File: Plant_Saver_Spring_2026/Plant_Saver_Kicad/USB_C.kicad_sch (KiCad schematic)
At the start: 3 parts, among them J3 54-00284

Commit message: Footprint correction
Changed the DHT20 from a header pin to the recommended SIP. Also had to reannotate in order to assign footprints.
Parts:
- removed J3: 54-00284, 54-00284:TENSILITY_54-00284, symbol USB-C Female Port:54-00284
- removed R32, R33: 5.1K, Resistor_THT:R_Axial_DIN0207_L6.3mm_D2.5mm_P10.16mm_Horizontal, symbol Device:R_US

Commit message: Fixed USB-C and Linear Regulator Sheetfiles
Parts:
- added J3: 54-00284, 54-00284:TENSILITY_54-00284, symbol USB-C Female Port:54-00284
- added R32, R33: 5.1K, Resistor_THT:R_Axial_DIN0207_L6.3mm_D2.5mm_P10.16mm_Horizontal, symbol Device:R_US
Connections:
- new net: J3.A5 (CC1), R32.1
- new net: J3.B5 (CC2), R33.1
- new net GND: J3.A12 (GND_A), J3.B12 (GND_B), R32.2, R33.2
- new net Vbus: J3.A9 (VBUS_A), J3.B9 (VBUS_B)

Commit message: Started PCB
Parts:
- added TP7: TestPoint, TestPoint:TestPoint_Pad_1.5x1.5mm, symbol Connector:TestPoint
- J8: renamed from J3; footprint 54-00284:TENSILITY_54-00284 -> 54_00284:TENSILITY_54-00284
- renumbered R32 to R5, R33 to R6
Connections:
- net Vbus: now also TP7.1
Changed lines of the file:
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@@
 		(color 0 0 0 0)
 	)
+	(junction
+		(at 173.99 86.36)
+		(diameter 0)
+		(color 0 0 0 0)
+	)
 	(wire
 		(pts
@@
 	(wire
 		(pts
+			(xy 173.99 86.36) (xy 175.26 86.36)
+		)
+		(stroke
+			(width 0)
+			(type default)
+		)
+	)
+	(wire
+		(pts
 			(xy 156.21 100.33) (xy 162.56 100.33)
 		)
@@
 	(wire
 		(pts
-			(xy 158.75 86.36) (xy 175.26 86.36)
+			(xy 158.75 86.36) (xy 173.99 86.36)
 		)
 		(stroke
@@
 		(pts
 			(xy 171.45 102.87) (xy 175.26 102.87)
+		)
+		(stroke
+			(width 0)
+			(type default)
+		)
+	)
+	(wire
+		(pts
+			(xy 173.99 86.36) (xy 173.99 88.9)
 		)
 		(stroke
@@
 			)
 			(justify left)
+		)
+	)
+	(symbol
+		(lib_id "Connector:TestPoint")
+		(at 173.99 88.9 180)
+		(unit 1)
+		(exclude_from_sim no)
+		(in_bom yes)
+		(on_board yes)
+		(dnp no)
+		(fields_autoplaced yes)
+		(property "Reference" "TP7"
+			(at 176.53 90.9319 0)
+			(effects
+				(font
+					(size 1.27 1.27)
+				)
+				(justify right)
+			)
+		)
+		(property "Value" "TestPoint"
+			(at 176.53 93.4719 0)
+			(effects
+				(font
+					(size 1.27 1.27)
+				)
+				(justify right)
+			)
+		)
+		(property "Footprint" "TestPoint:TestPoint_Pad_1.5x1.5mm"
+			(at 168.91 88.9 0)
+			(effects
+				(font
+					(size 1.27 1.27)
+				)
+				(hide yes)
+			)
+		)
+		(property "Datasheet" "~"
+			(at 168.91 88.9 0)
+			(effects
+				(font
+					(size 1.27 1.27)
+				)
+				(hide yes)
+			)
+		)
+		(property "Description" "test point"
+			(at 173.99 88.9 0)
+			(effects
+				(font
+					(size 1.27 1.27)
+				)
+				(hide yes)
+			)
+		)
+		(pin "1"
+		)
+		(instances
+			(project "Plant_Saver_Kicad"
+				(path "/7f244634-d37a-4ff0-ba36-8027330ab1bd/d7563033-ba85-41e2-802f-f59d27bfdb8e"
+					(reference "TP7")
+					(unit 1)
+				)
+			)
 		)
 	)
@@
 		(dnp no)
 		(fields_autoplaced yes)
-		(property "Reference" "J3"
+		(property "Reference" "J8"
 			(at 138.43 90.17 0)
 			(effects
@@
 			)
 		)
-		(property "Footprint" "54-00284:TENSILITY_54-00284"
+		(property "Footprint" "54_00284:TENSILITY_54-00284"
 			(at 138.43 100.33 0)
 			(effects
@@
 			(project "Plant_Saver_Dev"
 				(path "/7f244634-d37a-4ff0-ba36-8027330ab1bd/d7563033-ba85-41e2-802f-f59d27bfdb8e"
-					(reference "J3")
+					(reference "J8")
 					(unit 1)
 				)
@@
 		(dnp no)
 		(fields_autoplaced yes)
-		(property "Reference" "#PWR020"
+		(property "Reference" "#PWR014"
 			(at 175.26 110.49 0)
 			(effects
@@
 			(project "Plant_Saver_Dev"
 				(path "/7f244634-d37a-4ff0-ba36-8027330ab1bd/d7563033-ba85-41e2-802f-f59d27bfdb8e"
-					(reference "#PWR020")
+					(reference "#PWR014")
 					(unit 1)
 				)
@@
 		(dnp no)
 		(fields_autoplaced yes)
-		(property "Reference" "R33"
+		(property "Reference" "R6"
 			(at 173.99 97.7899 0)
 			(effects
@@
 			(project "Plant_Saver_Dev"
 				(path "/7f244634-d37a-4ff0-ba36-8027330ab1bd/d7563033-ba85-41e2-802f-f59d27bfdb8e"
-					(reference "R33")
+					(reference "R6")
 					(unit 1)
 				)
@@
 		(dnp no)
 		(fields_autoplaced yes)
-		(property "Reference" "R32"
+		(property "Reference" "R5"
 			(at 107.95 97.7899 0)
 			(effects
@@
 			(project "Plant_Saver_Dev"
 				(path "/7f244634-d37a-4ff0-ba36-8027330ab1bd/d7563033-ba85-41e2-802f-f59d27bfdb8e"
-					(reference "R32")
+					(reference "R5")
 					(unit 1)
 				)
@@
 		(dnp no)
 		(fields_autoplaced yes)
-		(property "Reference" "#PWR019"
+		(property "Reference" "#PWR013"
 			(at 102.87 110.49 0)
 			(effects
@@
 			(project "Plant_Saver_Dev"
 				(path "/7f244634-d37a-4ff0-ba36-8027330ab1bd/d7563033-ba85-41e2-802f-f59d27bfdb8e"
-					(reference "#PWR019")
-					(unit 1)
-				)
+					(reference "#PWR013")
+					(unit 1)
+				)

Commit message: Refined PCB layout
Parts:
- R5, R6: footprint Resistor_THT:R_Axial_DIN0207_L6.3mm_D2.5mm_P10.16mm_Horizontal -> Resistor_SMD:R_1206_3216Metric_Pad1.30x1.75mm_HandSolder
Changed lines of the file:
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@@
 			)
 		)
-		(property "Footprint" "Resistor_THT:R_Axial_DIN0207_L6.3mm_D2.5mm_P10.16mm_Horizontal"
+		(property "Footprint" "Resistor_SMD:R_1206_3216Metric_Pad1.30x1.75mm_HandSolder"
 			(at 172.466 99.314 90)
 			(effects
@@
 			)
 		)
-		(property "Footprint" "Resistor_THT:R_Axial_DIN0207_L6.3mm_D2.5mm_P10.16mm_Horizontal"
+		(property "Footprint" "Resistor_SMD:R_1206_3216Metric_Pad1.30x1.75mm_HandSolder"
 			(at 106.426 99.314 90)
 			(effects

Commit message: PCB Pre-Check complete
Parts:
- renumbered J8 to J9, R5 to R7, R6 to R8, TP7 to TP1
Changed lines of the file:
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@@
 		(dnp no)
 		(fields_autoplaced yes)
-		(property "Reference" "TP7"
+		(property "Reference" "TP1"
 			(at 176.53 90.9319 0)
 			(effects
@@
 			(project "Plant_Saver_Kicad"
 				(path "/7f244634-d37a-4ff0-ba36-8027330ab1bd/d7563033-ba85-41e2-802f-f59d27bfdb8e"
-					(reference "TP7")
+					(reference "TP1")
 					(unit 1)
 				)
@@
 		(dnp no)
 		(fields_autoplaced yes)
-		(property "Reference" "J8"
+		(property "Reference" "J9"
 			(at 138.43 90.17 0)
 			(effects
@@
 			(project "Plant_Saver_Dev"
 				(path "/7f244634-d37a-4ff0-ba36-8027330ab1bd/d7563033-ba85-41e2-802f-f59d27bfdb8e"
-					(reference "J8")
+					(reference "J9")
 					(unit 1)
 				)
@@
 		(dnp no)
 		(fields_autoplaced yes)
-		(property "Reference" "#PWR014"
+		(property "Reference" "#PWR015"
 			(at 175.26 110.49 0)
 			(effects
@@
 			(project "Plant_Saver_Dev"
 				(path "/7f244634-d37a-4ff0-ba36-8027330ab1bd/d7563033-ba85-41e2-802f-f59d27bfdb8e"
-					(reference "#PWR014")
+					(reference "#PWR015")
 					(unit 1)
 				)
@@
 		(dnp no)
 		(fields_autoplaced yes)
-		(property "Reference" "R6"
+		(property "Reference" "R8"
 			(at 173.99 97.7899 0)
 			(effects
@@
 			(project "Plant_Saver_Dev"
 				(path "/7f244634-d37a-4ff0-ba36-8027330ab1bd/d7563033-ba85-41e2-802f-f59d27bfdb8e"
-					(reference "R6")
+					(reference "R8")
 					(unit 1)
 				)
@@
 		(dnp no)
 		(fields_autoplaced yes)
-		(property "Reference" "R5"
+		(property "Reference" "R7"
 			(at 107.95 97.7899 0)
 			(effects
@@
 			(project "Plant_Saver_Dev"
 				(path "/7f244634-d37a-4ff0-ba36-8027330ab1bd/d7563033-ba85-41e2-802f-f59d27bfdb8e"
-					(reference "R5")
+					(reference "R7")
 					(unit 1)
 				)
@@
 		(dnp no)
 		(fields_autoplaced yes)
-		(property "Reference" "#PWR013"
+		(property "Reference" "#PWR014"
 			(at 102.87 110.49 0)
 			(effects
@@
 			(project "Plant_Saver_Dev"
 				(path "/7f244634-d37a-4ff0-ba36-8027330ab1bd/d7563033-ba85-41e2-802f-f59d27bfdb8e"
-					(reference "#PWR013")
-					(unit 1)
-				)
+					(reference "#PWR014")
+					(unit 1)
+				)

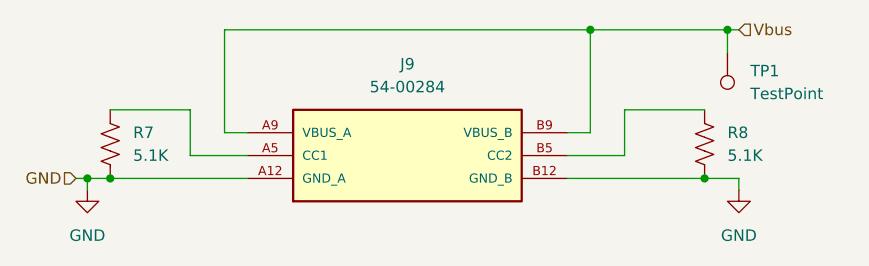
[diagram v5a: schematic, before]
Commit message: Finalizing checks/tweaks to PCB
Fixed a few footprint mask and silkscreen issues
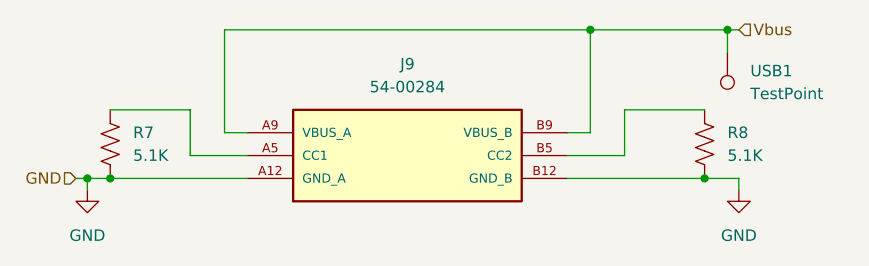
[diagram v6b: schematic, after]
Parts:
- renumbered TP1 to USB1
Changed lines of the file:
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@@
 		(dnp no)
 		(fields_autoplaced yes)
-		(property "Reference" "TP1"
+		(property "Reference" "USB1"
 			(at 176.53 90.9319 0)
 			(effects
@@
 			(project "Plant_Saver_Kicad"
 				(path "/7f244634-d37a-4ff0-ba36-8027330ab1bd/d7563033-ba85-41e2-802f-f59d27bfdb8e"
-					(reference "TP1")
+					(reference "USB1")
 					(unit 1)
 				)
